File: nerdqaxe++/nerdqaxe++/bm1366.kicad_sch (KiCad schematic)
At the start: 82 parts, among them U19 BM1370_mode1, U20 BM1370, U25 BM1370_mode1, U26 BM1370_mode1, U6 SN74AVC4T774, U8 25MHz

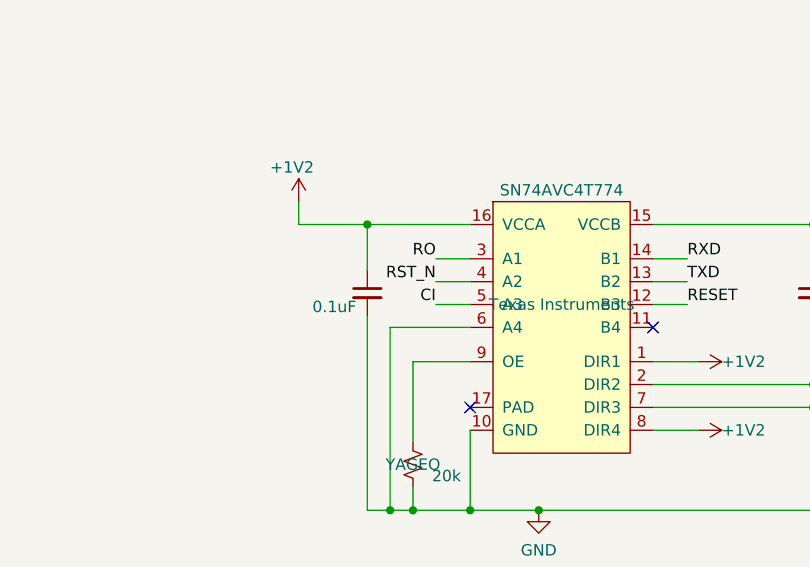
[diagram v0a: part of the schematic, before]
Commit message: fix level shifter
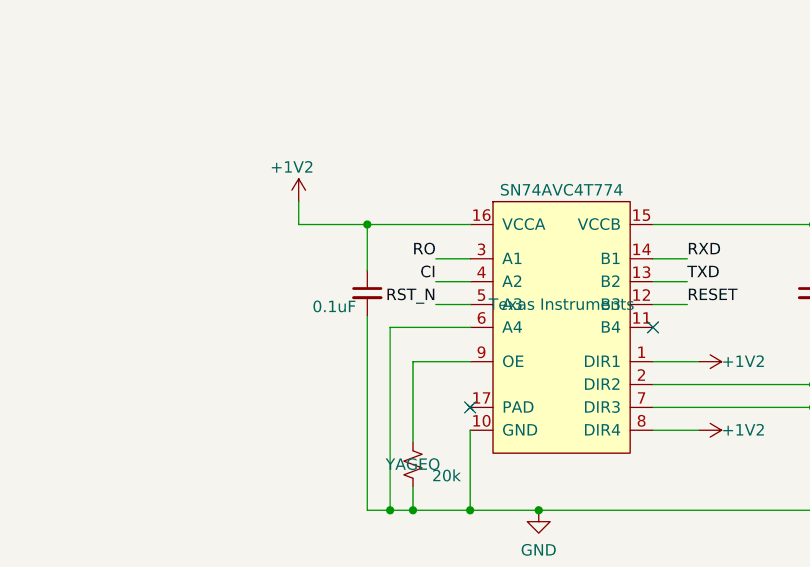
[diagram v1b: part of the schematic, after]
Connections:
- net CI: now also U6.4 (A2); no longer U6.5 (A3)
- net RST_N: now also U6.5 (A3); no longer U6.4 (A2)
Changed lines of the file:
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@@
 	)
 	(label "CI"
-		(at 337.82 134.62 180)
+		(at 337.82 132.08 180)
 		(effects
 			(font
@@
 			)
 			(justify left bottom)
+		)
+	)
+	(label "RST_N"
+		(at 337.82 134.62 180)
+		(effects
+			(font
+				(size 1.27 1.27)
+			)
+			(justify right bottom)
 		)
 	)
@@
 		)
 	)
-	(label "RST_N"
-		(at 337.82 132.08 180)
-		(effects
-			(font
-				(size 1.27 1.27)
-			)
-			(justify right bottom)
-		)
-	)

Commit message: clean DRC (incomplete)
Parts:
- removed C127, C128, C131, C132, C133, C134, C136, C137, C138, C139, C140, C81: 10uF, Capacitor_SMD:C_0603_1608Metric, symbol Device:C_Small
- removed C25: 100nF, Capacitor_SMD:C_0402_1005Metric, symbol Device:C
- removed C28, C30, C32, C34, C35, C36, C37, C40, C42, C43, C44, C47, C50, C51, C52, C54, C56, C57, C58, C60, C62, C63, C64, C66, C67, C68, C69, C70, C71, C72, C73, C74, C75, C76, C77, C78, C79, C80, C93, C94: 1µF, Capacitor_SMD:C_0402_1005Metric, symbol Device:C
- removed C59: 0.1uF, Capacitor_SMD:C_0402_1005Metric, symbol Device:C_Small
- removed R19, R20, R21, R22, R23: 10k, Resistor_SMD:R_0402_1005Metric, symbol Device:R
- removed R26: 20k, Resistor_SMD:R_0402_1005Metric, symbol Device:R_Small_US
- removed R44, R45, R46, R47: 1k, Resistor_SMD:R_0402_1005Metric, symbol Device:R
- removed R49, R50, R51: 2k, Resistor_SMD:R_0402_1005Metric, symbol Device:R
- removed U19, U25, U26: BM1370_mode1, qaxe:BM1370, symbol mylib7:BM1368_mode1
- removed U20: BM1370, qaxe:BM1370, symbol mylib7:BM1368_mode1
- removed U6: SN74AVC4T774, qaxe:BQB0016A-MFG, symbol bitaxe:SN74AVC4T774-BQB
- added A1, A3: BM1370, bitaxe:BM1370, symbol bitaxe:BM1370_mode1
- added A4, A6: BM1370, bitaxe:BM1370, symbol bitaxe:BM1370_mode0
- added C101, C107, C120, C121, C122, C123, C153, C154, C155, C156, C157, C158, C159, C160, C161, C162, C163, C166, C171, C172, C177, C178, C179, C180, C181, C182, C183, C184, C185, C186, C187, C188, C189, C190, C191, C192, C193, C194, C92, C93, C94: 1uF, Capacitor_SMD:C_0402_1005Metric, symbol Device:C_Small
- added C105, C108, C109, C114, C115, C116, C117, C118, C119, C164, C165, C167, C168, C169, C170, C173, C174, C175, C176: 10uF, Capacitor_SMD:C_0603_1608Metric, symbol Device:C_Small
- added C87: 0.1uF, Capacitor_SMD:C_0402_1005Metric, symbol Device:C_Small
- added R23: 20k, Resistor_SMD:R_0402_1005Metric, symbol Device:R_Small_US
- added R24, R29, R41, R42: 10k, Resistor_SMD:R_0402_1005Metric, symbol Device:R_US
- added R26, R28, R43, R44: 1k, Resistor_SMD:R_0402_1005Metric, symbol Device:R_US
- added R39, R40, R45: 2k, Resistor_SMD:R_0402_1005Metric, symbol Device:R_US
- added R46: 0, Resistor_SMD:R_0402_1005Metric, symbol Device:R_US
- added U10, U11: MCP1824T-1202E/OT, Package_TO_SOT_SMD:SOT-23-5, symbol bitaxe:MCP1824
- added U12, U13: MCP1824T-0802E, Package_TO_SOT_SMD:SOT-23-5, symbol bitaxe:MCP1824
- added U7: SN74AXC4T774, bitaxe:BQB0016A-MFG, symbol bitaxe:SN74AVC4T774-BQB
- added U9: 25MHz, Oscillator:Oscillator_SMD_EuroQuartz_XO32-4Pin_3.2x2.5mm, symbol Oscillator:ASDMB-xxxMHz
- C100: value 0.1uF -> 10uF; footprint Capacitor_SMD:C_0402_1005Metric -> Capacitor_SMD:C_0603_1608Metric; DK 478-KGM05AR71C104KHCT-ND -> (none); LCSC (none) -> C92487 Hot; PARTNO KGM05AR71C104KH -> CL10A106MO8NQNC
- C86: value 10uF -> 0.1uF; footprint Capacitor_SMD:C_0603_1608Metric -> Capacitor_SMD:C_0402_1005Metric; DK (none) -> 478-KGM05AR71C104KHCT-ND; LCSC C92487 Hot -> (none); Manufacturer  Samsung Electro-Mechanics -> (none); PARTNO CL10A106MO8NQNC -> KGM05AR71C104KH
- C89, C90, C91, C95, C97, C98, C99: value 10uF -> 1uF; footprint Capacitor_SMD:C_0603_1608Metric -> Capacitor_SMD:C_0402_1005Metric; LCSC C92487 Hot -> C29266; Manufacturer  Samsung Electro-Mechanics -> (none); PARTNO CL10A106MO8NQNC -> CL05A105KO5NNNC
- U8: Manufacturer  Shenzhen SCTF Elec -> (none)
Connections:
- net +3V3: now also C87.1, U7.15 (VCCB); no longer C100.1
- net BI: now also A1.9 (BI), R29.2
- net CI: now also A1.6 (CI), U7.4 (A2)
- net CLKI: now also A1.8 (CLKI)
- net GND: now also C90.1, A1.13 (PLL_VSS), A1.18 (VSS), A1.27 (VSS), A1.32 (VSS), A1.4 (VSS), A3.13 (PLL_VSS), A3.18 (VSS), A3.27 (VSS), A3.32 (VSS), A3.4 (VSS), C108.2, C114.2, C116.2, C118.2, C121.2, C122.2, C154.1, C158.2, C160.2, C164.2, C167.2, C169.2, C173.2, C175.2, C180.2, C182.2, C186.2, C187.1, C189.1, C191.1, C193.1, C87.2, C94.2, R23.1, R28.2, R29.1, R40.1, R44.2, U10.2 (GND), U12.2 (GND), U7.1 (DIR1), U7.10 (GND), U7.2 (DIR2), U7.6 (A4); no longer C89.2, C90.2, C91.2, C95.2, C97.2, C98.2
- net RESET: now also U7.14 (B1)
- net RO: now also A1.7 (RO), U7.5 (A3)
- net RST_N: now also A1.5 (NRSTI), U7.3 (A1)
- net RXD: now also U7.12 (B3)
- net TXD: now also U7.13 (B2)
- net VDD: now also A4.31 (VDD), A6.31 (VDD), C101.2, C105.1, C109.1, C115.1, C117.1, C119.1, C163.2, C165.1, C168.1, C170.1, C171.1, C174.1, C176.1; no longer C86.1, C89.1, C90.1, C91.1, C95.1, C97.1, C98.1, C99.1
- net +1V2 renamed 1V2_0
- net 1V2_0: now also C86.1, C99.1, A1.15 (VDDIO_12_0), A3.16 (VDDIO_12_1), C182.1, C189.2, R41.2, U10.5 (VOUT), U7.16 (VCCA), U7.7 (DIR3), U7.8 (DIR4)
- new net: A4.9 (NRSTO), A6.22 (NRSTI), R39.2
- new net: A4.7 (RI), A6.24 (RO), R42.1
- new net: A6.3 (VDD1_0), C89.2, C91.1
- new net: A4.14 (VDDIO_08_0), A6.17 (VDDIO_08_1), C123.1, C157.1
- new net: A1.1 (VDD3_0), C107.1, C98.2
- new net: A1.11 (LITE_PAD), R28.1
- new net: A1.14 (VDDIO_08_0), C94.1
- new net: A1.16 (VDDIO_12_1), A3.15 (VDDIO_12_0), C121.1, C160.1
- new net: A1.17 (VDDIO_08_1), A3.14 (VDDIO_08_0), C122.1, C158.1
- new net: A1.2 (VDD2_0), C92.2, C98.1
- new net: A1.22 (BO), A3.9 (BI)
- new net: A1.23 (CLKO), A3.8 (CLKI)
- new net: A1.24 (RI), A3.7 (RO), R41.1
- new net: A1.25 (CO), A3.6 (CI)
- new net: A1.26 (NRSTO), A3.5 (NRSTI), R40.2
- new net: A1.28 (VDD1_1), A3.3 (VDD1_0), C154.2, C156.1
- new net: A1.29 (VDD2_1), A3.2 (VDD2_0), C156.2, C162.1
- new net: A1.3 (VDD1_0), C90.2, C92.1
- new net: A1.30 (VDD3_1), A3.1 (VDD3_0), C162.2, C166.1
- new net: A3.29 (VDD2_1), C178.2, C184.1
- new net: A3.28 (VDD1_1), C184.2, C186.1
- new net: A4.29 (VDD2_1), C177.2, C183.1
- new net: A4.28 (VDD1_1), C183.2, C185.1
- new net: A3.11 (LITE_PAD), R44.1
- new net: A4.15 (VDDIO_12_0), A6.16 (VDDIO_12_1), C120.1, C161.1
- new net: A6.1 (VDD3_0), C101.1, C95.2
- new net: A6.11 (LITE_PAD), R26.1
- new net: A6.14 (VDDIO_08_0), C93.1
- new net: A6.15 (VDDIO_12_0), C97.1
- new net: A6.2 (VDD2_0), C91.2, C95.1
- new net: A4.8 (CO), A6.23 (CI)
- new net: A4.6 (CLKO), A6.25 (CLKI)
- new net: A4.5 (BO), A6.26 (BI)
- new net: A4.3 (VDD1_0), A6.28 (VDD1_1), C153.2, C155.1
- new net: A4.2 (VDD2_0), A6.29 (VDD2_1), C155.2, C159.1
- new net: A4.1 (VDD3_0), A6.30 (VDD3_1), C159.2, C163.1
- new net: A6.7 (RI), R24.1
- new net: A3.30 (VDD3_1), C172.2, C178.1
- new net: A4.30 (VDD3_1), C171.2, C177.1
- new net: A4.11 (LITE_PAD), R43.1
- new net: R46.2, U9.3 (Out)
- new net: R23.2, U7.9 (OE)
- new net +5V: C187.2, C188.2, C191.2, C192.2, U10.1 (VIN), U10.3 (EN), U11.1 (VIN), U11.3 (EN), U12.1 (VIN), U12.3 (EN), U13.1 (VIN), U13.3 (EN)
- new net 0V8_0: A3.17 (VDDIO_08_1), C180.1, C193.2, U12.5 (VOUT)
- new net 0V8_1: A4.17 (VDDIO_08_1), C179.1, C194.2, U13.5 (VOUT)
- new net 1V2_1: A4.16 (VDDIO_12_1), C181.1, C190.2, R24.2, R42.2, U11.5 (VOUT), U9.1 (Standby), U9.4 (VDD)
- new net GND_1: A1.31 (VDD), A3.31 (VDD), A4.13 (PLL_VSS), A4.18 (VSS), A4.19 (PIN_MODE), A4.27 (VSS), A4.32 (VSS), A4.4 (VSS), A6.13 (PLL_VSS), A6.18 (VSS), A6.19 (PIN_MODE), A6.27 (VSS), A6.32 (VSS), A6.4 (VSS), C100.1, C105.2, C107.2, C108.1, C109.2, C114.1, C115.2, C116.1, C117.2, C118.1, C119.2, C120.2, C123.2, C153.1, C157.2, C161.2, C164.1, C165.2, C166.2, C167.1, C168.2, C169.1, C170.2, C172.1, C173.1, C174.2, C175.1, C176.2, C179.2, C181.2, C185.2, C188.1, C190.1, C192.1, C194.1, C89.1, C93.2, C97.2, R26.2, R39.1, R43.2, R45.1, U11.2 (GND), U13.2 (GND), U9.2 (GND)
- new net Level Shifter/BI: A3.22 (BO)
- new net Level Shifter/BO: A4.26 (BI)
- new net Level Shifter/CI: A3.25 (CO)
- new net Level Shifter/CLKI: A3.23 (CLKO)
- new net Level Shifter/CLKO: A4.25 (CLKI), R46.1
- new net Level Shifter/CO: A4.23 (CI)
- new net Level Shifter/NRSTI: A3.26 (NRSTO)
- new net Level Shifter/NRSTO: A4.22 (NRSTI), R45.2
- new net Level Shifter/RI: A4.24 (RO)
- new net Level Shifter/RO: A3.24 (RI)
- new net TEMP1_N: A1.21 (TEMP_N)
- new net TEMP1_P: A1.20 (TEMP_P)
- no-connect marks 26 -> 25
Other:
- added sheet Level Shifter (level_shifter.kicad_sch)
- note added: "->"
- note added: "<-"
- note added: "Direction Control HIGH= A -> B LOW = A <- B"
- note added: "Optional 2nd domain clock if we can't get clock level shifting working"

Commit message: change level shifter package
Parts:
- U7: footprint bitaxe:BQB0016A-MFG -> Package_SO:TSSOP-16_4.4x5mm_P0.65mm
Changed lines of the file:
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@@
 			)
 		)
-		(property "Footprint" "bitaxe:BQB0016A-MFG"
+		(property "Footprint" "Package_SO:TSSOP-16_4.4x5mm_P0.65mm"
 			(at 468.122 242.57 0)
 			(hide yes)

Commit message: Rev7 complete
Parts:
- removed C114, C115, C169, C170: 10uF, Capacitor_SMD:C_0603_1608Metric, symbol Device:C_Small
- added C22, C23, C25, C28: 100nf, Capacitor_SMD:C_0402_1005Metric, symbol Device:C_Small
- added C47, C50, C51, C52: 33pF, Capacitor_SMD:C_0402_1005Metric, symbol Device:C_Small
- R46: PARTNO (none) -> RC0402JR-070RL
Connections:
- net GND: now also C25.1, C28.1, C51.1, C52.1
- net GND_1: now also C22.1, C23.1, C25.2, C28.2, C47.1, C50.1, C51.2, C52.2
- net VDD: now also C22.2, C23.2, C47.2, C50.2
